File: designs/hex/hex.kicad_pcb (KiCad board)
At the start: 2 copper layers, 50 x 50 mm, 32 parts, among them IC1 ATMEGA1284P-P, K1 RESONATOR, K2 REGUL, P1 PROG, P2 XBEE, P3 BATT (4.8V-6V), P4 DPDT, P5 CONN_6, P6 CONN_1

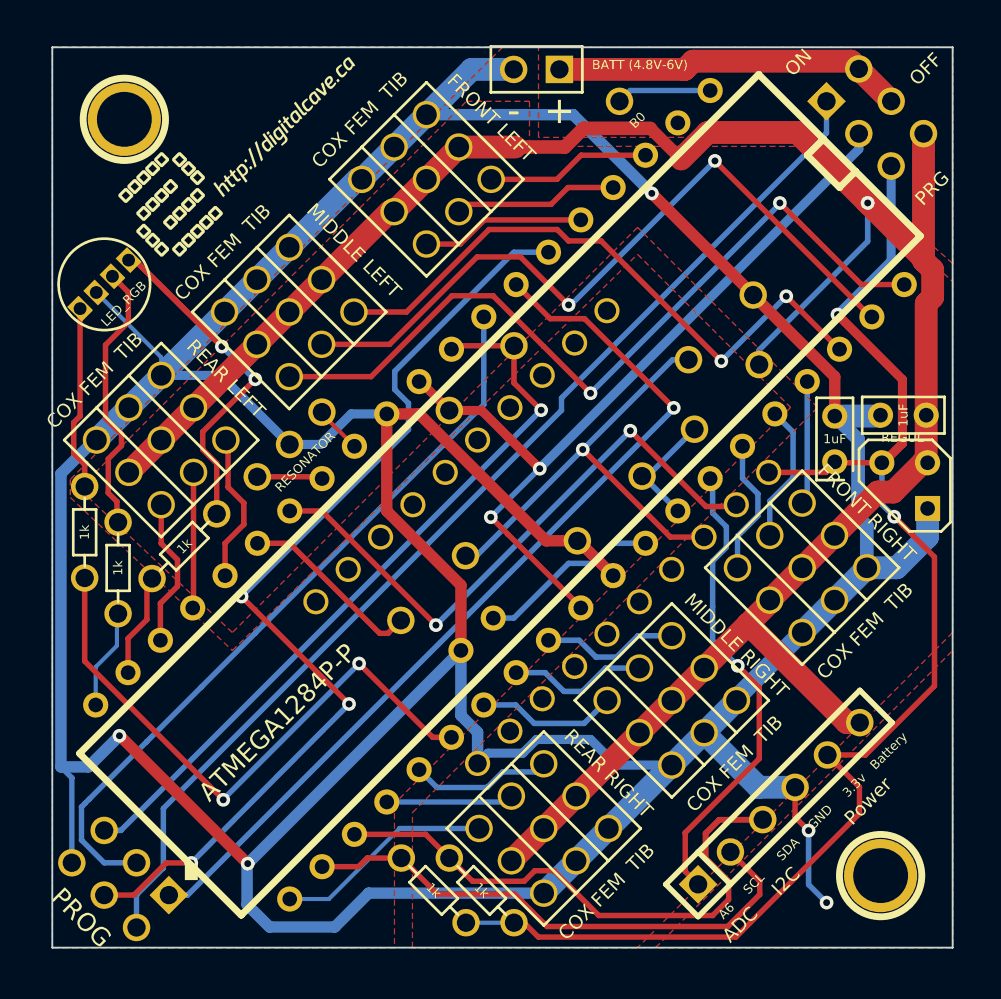
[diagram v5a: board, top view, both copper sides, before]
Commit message: Some more footprint and ground / power cleanup
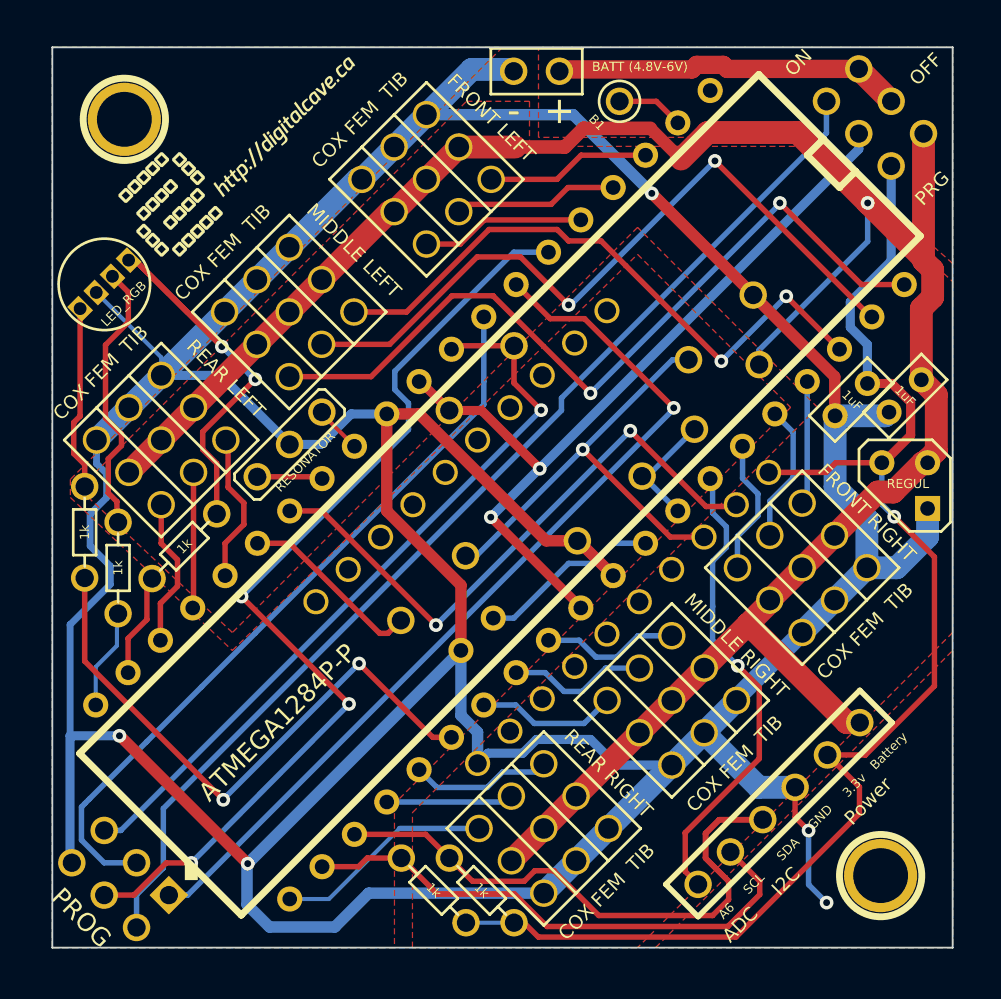
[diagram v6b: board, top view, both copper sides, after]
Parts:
- moved C3 2.37 mm to (169.4, 64.6), turned to 225 degrees
- moved C2 1.07 mm to (172.4, 64.4), turned to 45 degrees
- moved P3 0.10 mm to (151.9, 46.3)
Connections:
- IC1 pad 1: N-0000018 -> (no net)
- IC1 pad 2: (no net) -> N-0000018
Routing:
- net N-0000018: track 5.28 -> 3.73 mm
- net SWITCHED_BATTERY: track 127.2 -> 127.9 mm
- net VCC_3v3: track 76.4 -> 77.0 mm, vias 2 -> 1
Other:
- board text added: "B1"
- board text removed: "B0"

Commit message: Another complete do-over... this time replacing the XBee breakout module with a real XBee (no point having a breakout on a printed board), and improving pin mapping for better routing.  All high current routes are 50mil, all low current power routes are 15mil, and the rest are 10mil.
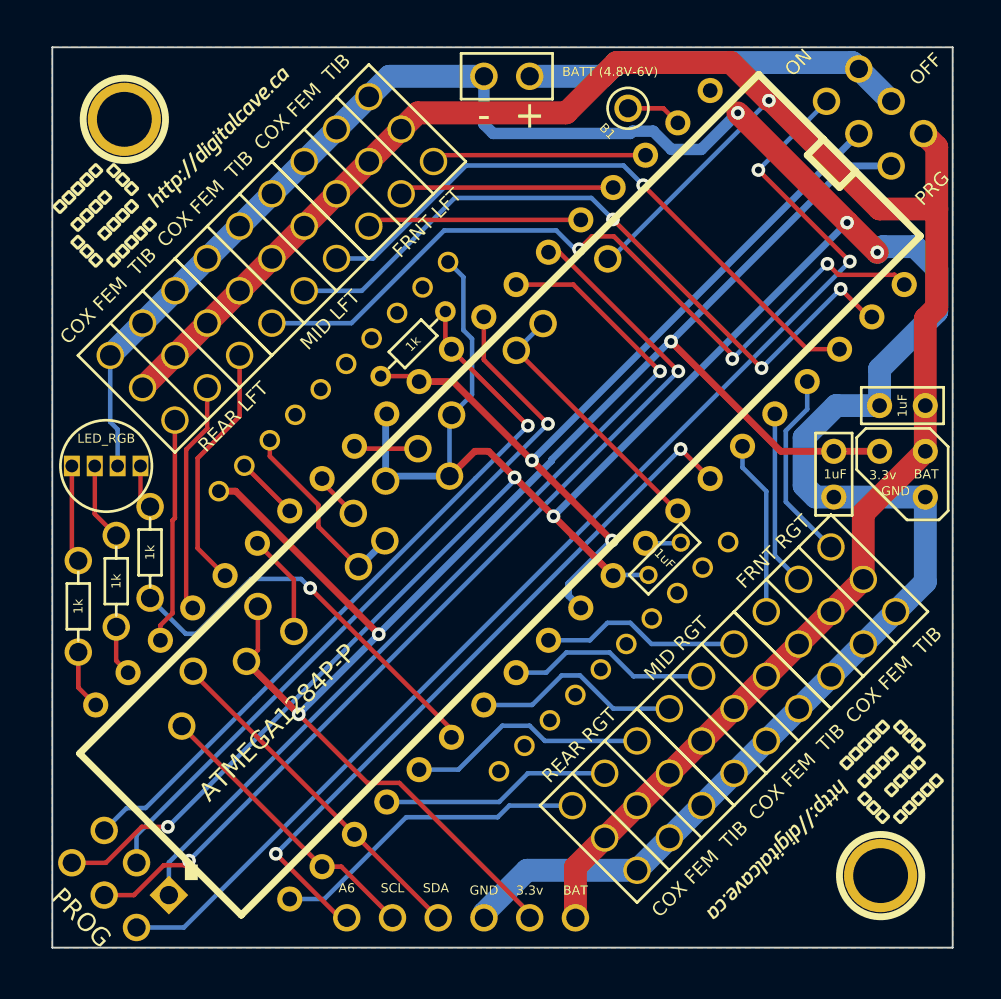
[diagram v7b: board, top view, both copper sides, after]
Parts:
- added ?: , digitalcave_logo_wide_small, F.Cu at (167.9, 88.9)
- C1, R1: moved to F.Cu
- K1, R7, R8: moved to B.Cu
- S1: value FRONT LEFT -> FRNT LFT
- S2: value FRONT RIGHT -> FRNT RGT
- S3: value MIDDLE LEFT -> MID LFT
- S4: value MIDDLE RIGHT -> MID RGT
- S5: value REAR LEFT -> REAR LFT
- S6: value REAR RIGHT -> REAR RGT
- moved R7 19.9 mm to (134.6, 77.9), turned to 225 degrees
- moved D1 19.6 mm to (145.3, 70.6)
- moved P5 18.8 mm to (147.7, 93.3), turned to 0 degrees
- moved R8 16.4 mm to (134.0, 80.9), turned to 225 degrees
- moved C1 11.2 mm to (159.0, 73.4)
- moved R2 10.3 mm to (154.1, 58.5)
- moved L1 10.1 mm to (128.0, 68.2), turned to 180 degrees
- moved R3 9.88 mm to (149.0, 63.6)
- moved R5 6.77 mm to (126.4, 76.0), turned to 90 degrees
- moved R9 5.97 mm to (140.2, 75.6)
- moved K1 5.71 mm to (143.5, 69.1)
- moved S6 5.33 mm to (155.7, 88.0)
- moved S5 4.76 mm to (133.6, 61.2)
- moved R1 4.26 mm to (145.0, 61.5)
- moved C3 4.25 mm to (168.4, 68.7), turned to 270 degrees
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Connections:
- IC1 pad 19: LED_GREEN -> LED_BLUE
- IC1 pad 20: LED_BLUE -> LED_GREEN
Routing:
- net GND: track 265.2 -> 218.8 mm, vias 5 -> 6
- net AVR_RX: track 33.7 -> 3.56 mm, vias 2 -> 0
- net LED_GREEN_R: track 29.7 -> 5.41 mm, vias 2 -> 0
- net I2C_SDA: track 40.2 -> 19.3 mm
- net VCC_3v3: track 77.0 -> 97.0 mm, vias 1 -> 3
- net LED_RED: track 38.8 -> 22.7 mm, vias 2 -> 1
- net AVR_TX: track 25.6 -> 11.2 mm, vias 1 -> 0
- net I2C_SCL: track 29.9 -> 16.1 mm
- net ADC6: track 26.3 -> 39.5 mm, vias 1 -> 2
- net LED_BLUE_R: track 15.4 -> 4.36 mm
- net AREF: track 10.2 -> 1.97 mm
- net SWITCHED_BATTERY: track 127.9 -> 119.8 mm
- net ADC_BATTERY_METER: track 6.78 -> 14.8 mm
- net LED_RED_R: track 10.3 -> 2.48 mm
- net PWM17: track 12.1 -> 17.8 mm
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- removed copper zone on F.Cu, net BATTERY
- removed copper zone on F.Cu, net GND
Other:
- net class Default: trace_width 0.3048 -> 0.254
- rule trace_min: 0.2286 -> 0.2032
- board text added: "BAT"
- board text removed: "ADC"
- board text removed: "Battery"
- board text removed: "I2C"
- board text removed: "Power"
- board text removed: "RX"
- board text removed: "TX"

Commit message: Changed the front plane to GND
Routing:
- added copper zone on F.Cu, net GND
- removed copper zone on F.Cu, net SWITCHED_BATTERY
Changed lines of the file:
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@@
-(kicad_pcb (version 3) (host pcbnew "(2013-dec-23)-stable")
+(kicad_pcb (version 3) (host pcbnew "(2014-01-10 BZR 4027)-stable")
   (general
     (links 109)
@@
     )
   )
-  (zone (net 42) (net_name SWITCHED_BATTERY) (layer F.Cu) (hatch edge 0.508)
+  (zone (net 7) (net_name GND) (layer F.Cu) (hatch edge 0.508)
     (connect_pads (clearance 0.3302))
     (min_thickness 0.3302)
